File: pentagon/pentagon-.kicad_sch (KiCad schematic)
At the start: 28 parts, among them J1 Conn_01x05_Pin, J2 Conn_01x05_Pin, J3 Conn_01x05_Pin, J4 Conn_01x05_Pin, J5 Conn_01x05_Pin

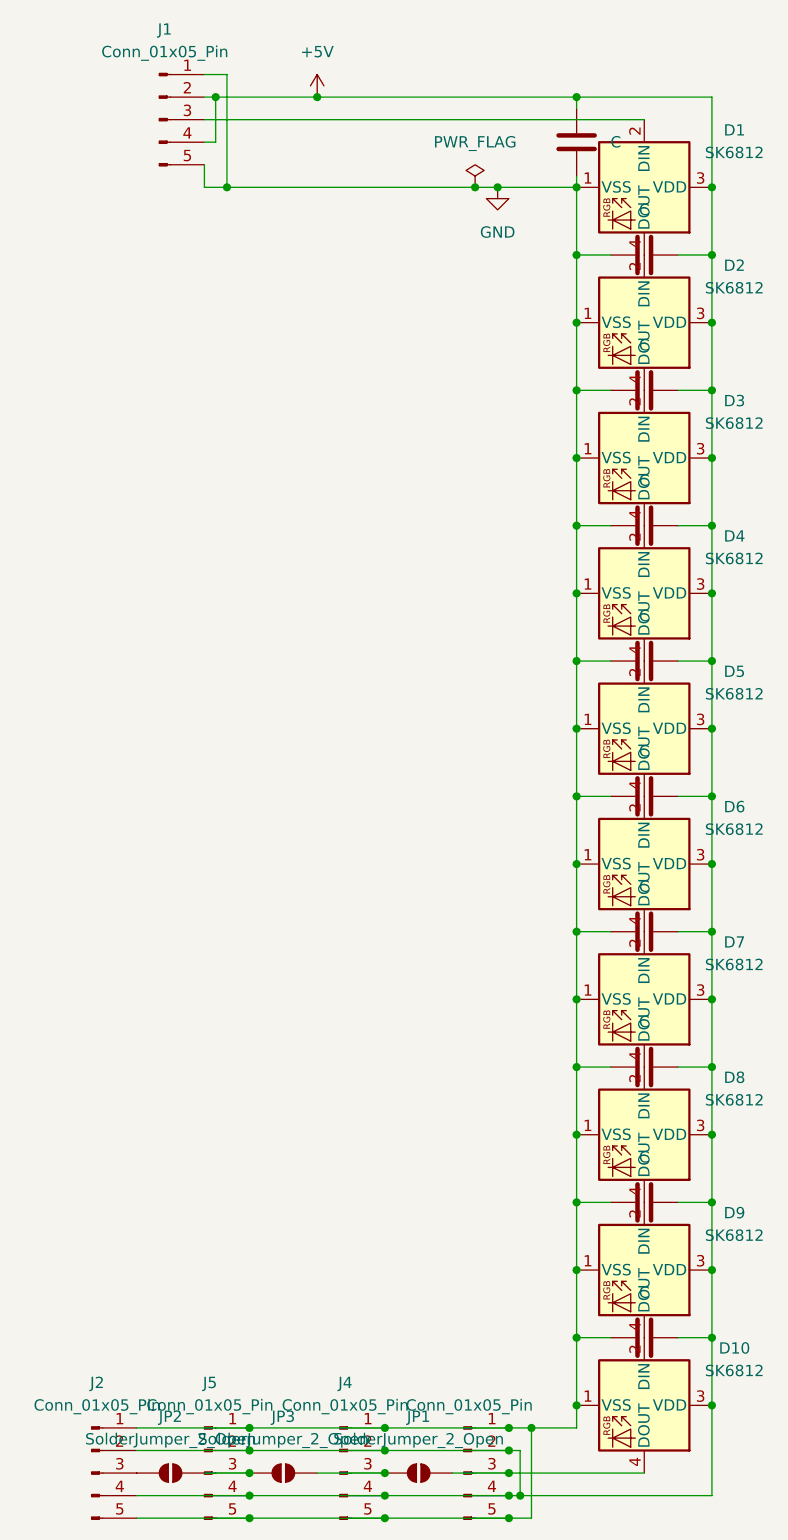
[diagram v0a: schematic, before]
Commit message: added mic to antenna, decagons, octagons and all the shenanigans
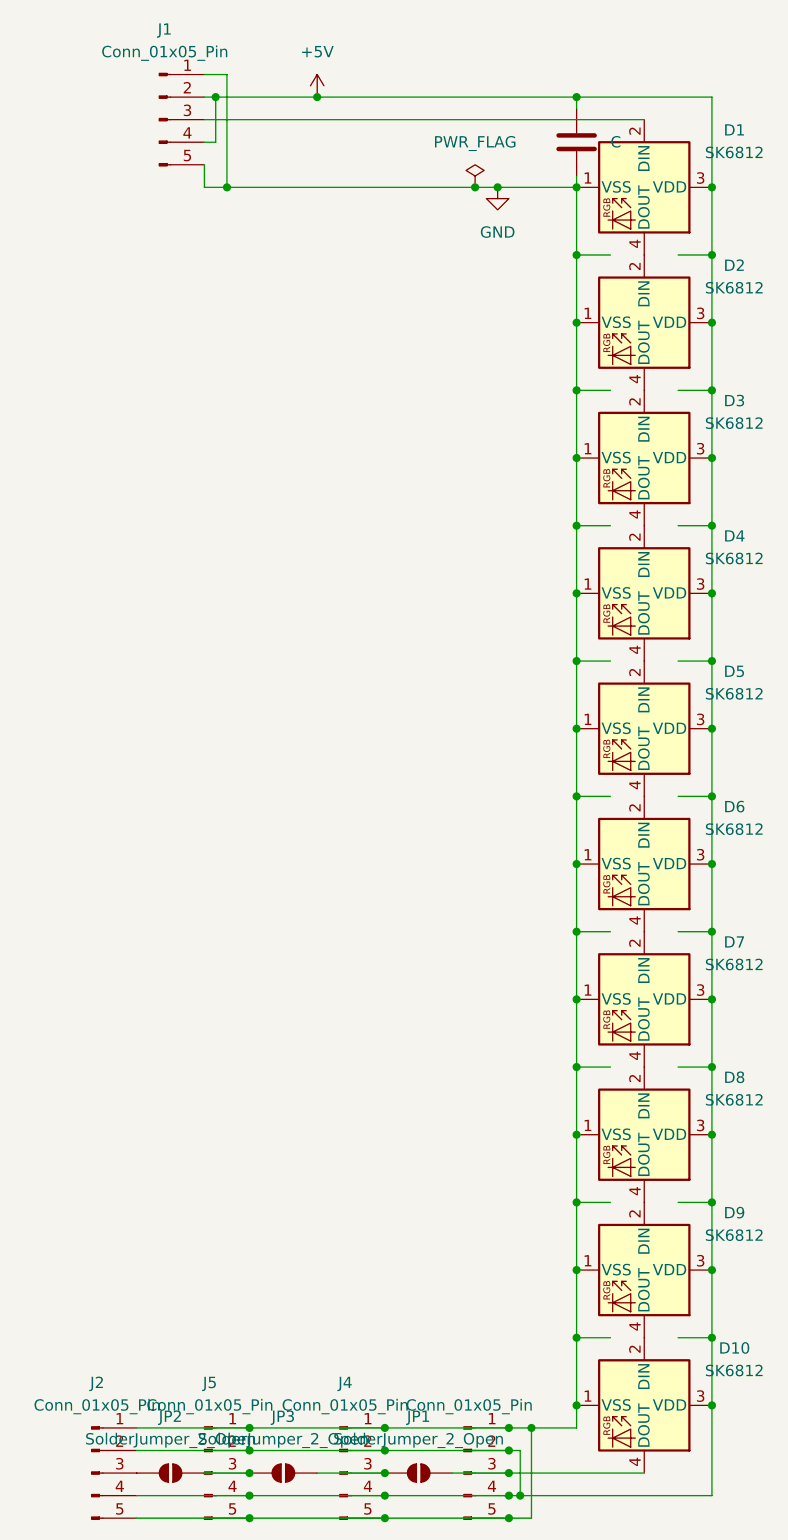
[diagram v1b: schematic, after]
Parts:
- removed C10, C2, C3, C4, C5, C6, C7, C8, C9: C, Capacitor_SMD:C_0805_2012Metric_Pad1.18x1.45mm_HandSolder, symbol Device:C
- J1, J2, J3, J4, J5: footprint Connector_PinHeader_2.54mm:PinHeader_1x05_P2.54mm_Vertical -> Connector_PinSocket_2.54mm:PinSocket_1x05_P2.54mm_Vertical
